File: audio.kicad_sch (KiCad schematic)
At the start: 15 parts, among them J5 FH34SRJ-6S-0.5SH(50), J6 FH34SRJ-6S-0.5SH(50), J7 Conn_01x02_Female, U6 ALC5672

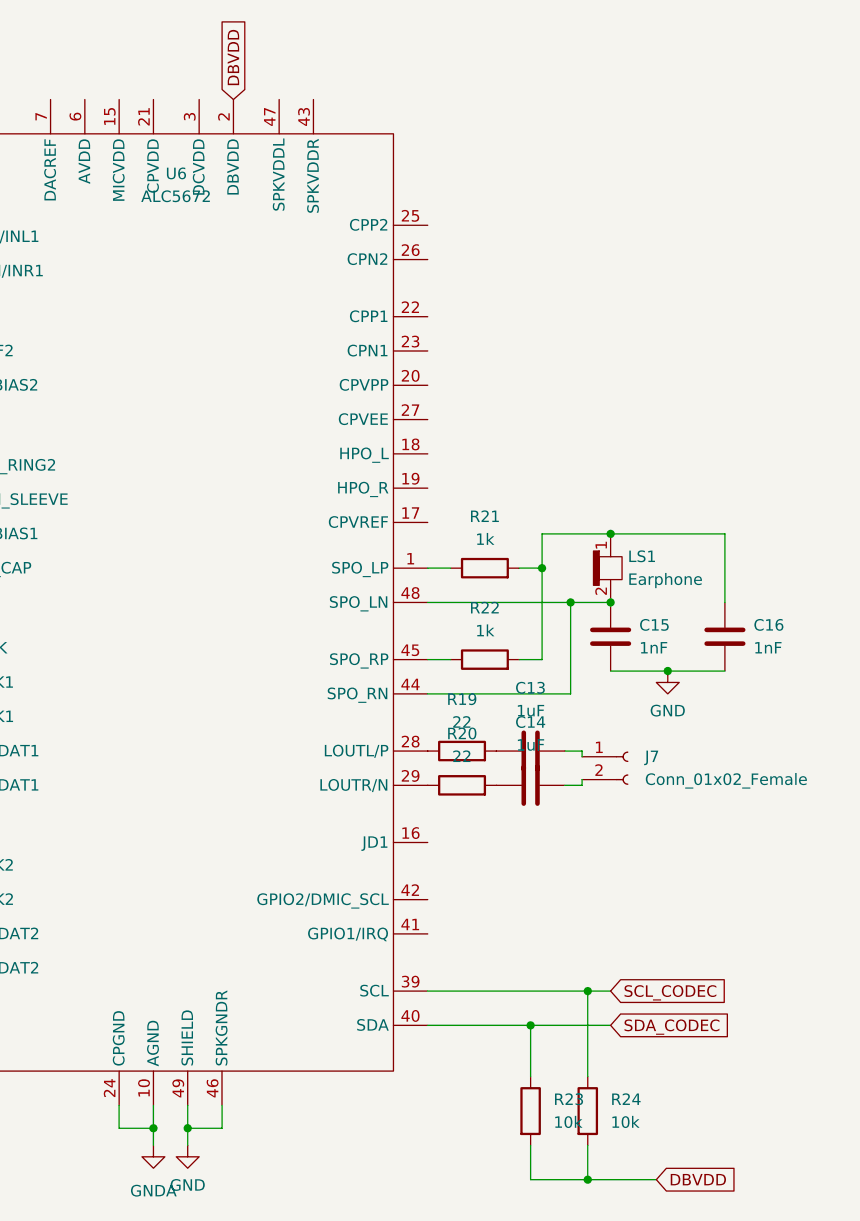
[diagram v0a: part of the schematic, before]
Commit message: USB IC Removal
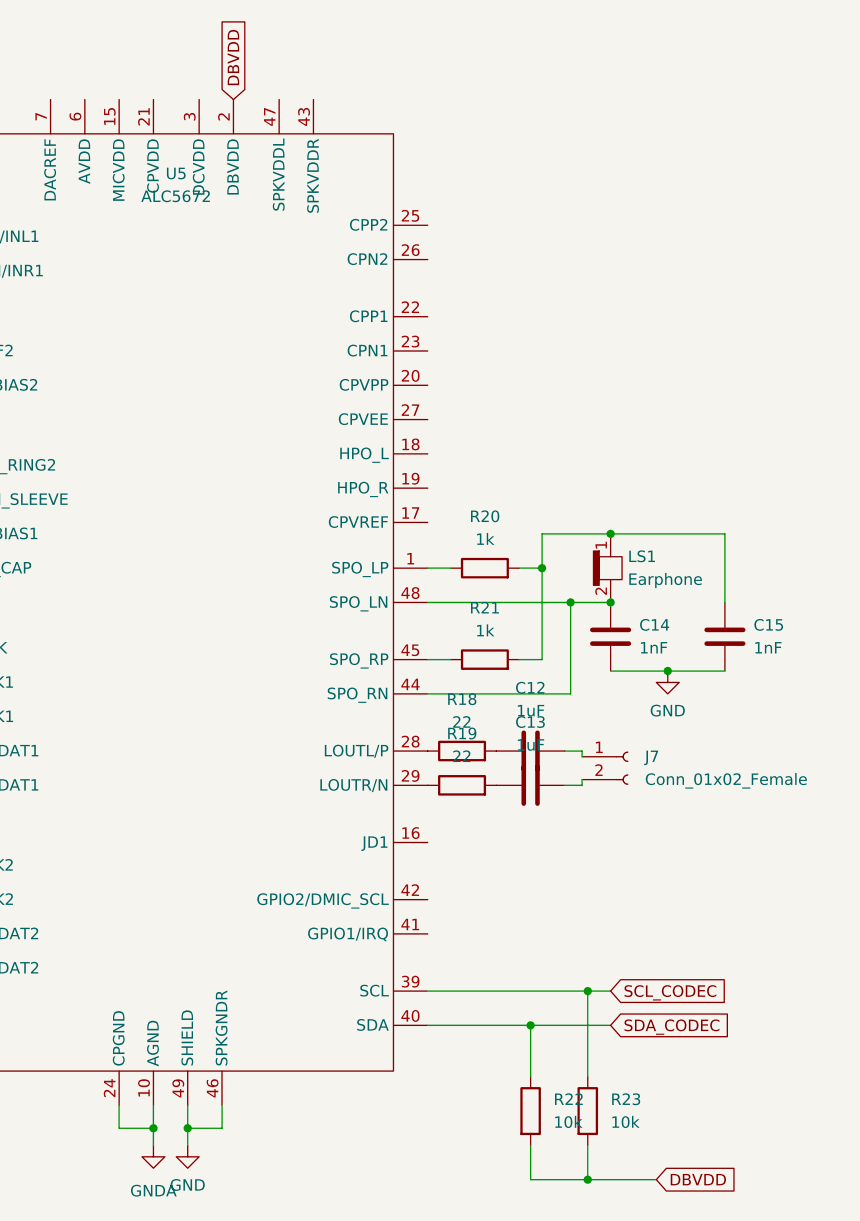
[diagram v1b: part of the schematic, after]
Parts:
- renumbered C13 to C12, C14 to C13, C15 to C14, C16 to C15, R19 to R18, R20 to R19, R21 to R20, R22 to R21, R23 to R22, R24 to R23, U6 to U5
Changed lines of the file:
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@@
   (symbol (lib_id "power:GND") (at 153.035 68.58 0) (unit 1)
     (in_bom yes) (on_board yes) (fields_autoplaced)
-    (property "Reference" "#PWR044" (id 0) (at 153.035 74.93 0)
+    (property "Reference" "#PWR041" (id 0) (at 153.035 74.93 0)
       (effects (font (size 1.27 1.27)) hide)
     )
@@
   (symbol (lib_id "Device:C") (at 256.54 100.965 90) (unit 1)
     (in_bom yes) (on_board yes) (fields_autoplaced)
-    (property "Reference" "C13" (id 0) (at 256.54 93.98 90))
+    (property "Reference" "C12" (id 0) (at 256.54 93.98 90))
     (property "Value" "1uF" (id 1) (at 256.54 96.52 90))
     (property "Footprint" "Capacitor_SMD:C_0402_1005Metric" (id 2) (at 260.35 99.9998 0)
@@
   (symbol (lib_id "Device:C") (at 256.54 104.775 90) (unit 1)
     (in_bom yes) (on_board yes) (fields_autoplaced)
-    (property "Reference" "C14" (id 0) (at 256.54 97.79 90))
+    (property "Reference" "C13" (id 0) (at 256.54 97.79 90))
     (property "Value" "1uF" (id 1) (at 256.54 100.33 90))
     (property "Footprint" "Capacitor_SMD:C_0402_1005Metric" (id 2) (at 260.35 103.8098 0)
@@
   (symbol (lib_id "Device:R") (at 251.46 80.645 90) (unit 1)
     (in_bom yes) (on_board yes) (fields_autoplaced)
-    (property "Reference" "R21" (id 0) (at 251.46 74.93 90))
+    (property "Reference" "R20" (id 0) (at 251.46 74.93 90))
     (property "Value" "1k" (id 1) (at 251.46 77.47 90))
     (property "Footprint" "Resistor_SMD:R_0402_1005Metric" (id 2) (at 251.46 82.423 90)
@@
   (symbol (lib_id "JLCPCB:ALC5672") (at 217.17 81.915 0) (unit 1)
     (in_bom yes) (on_board yes) (fields_autoplaced)
-    (property "Reference" "U6" (id 0) (at 217.17 36.83 0))
+    (property "Reference" "U5" (id 0) (at 217.17 36.83 0))
     (property "Value" "ALC5672" (id 1) (at 217.17 39.37 0))
     (property "Footprint" "JLCPCB:ALC5672-VB-CGT_QFN-48_EP_6x6_Pitch0.4mm" (id 2) (at 217.17 123.14 0)
@@
   (symbol (lib_id "power:GND") (at 132.715 71.12 0) (unit 1)
     (in_bom yes) (on_board yes) (fields_autoplaced)
-    (property "Reference" "#PWR042" (id 0) (at 132.715 77.47 0)
+    (property "Reference" "#PWR039" (id 0) (at 132.715 77.47 0)
       (effects (font (size 1.27 1.27)) hide)
     )
@@
   (symbol (lib_id "power:GND") (at 153.67 34.925 0) (unit 1)
     (in_bom yes) (on_board yes) (fields_autoplaced)
-    (property "Reference" "#PWR046" (id 0) (at 153.67 41.275 0)
+    (property "Reference" "#PWR043" (id 0) (at 153.67 41.275 0)
       (effects (font (size 1.27 1.27)) hide)
     )
@@
   (symbol (lib_id "power:GND") (at 218.44 144.78 0) (unit 1)
     (in_bom yes) (on_board yes) (fields_autoplaced)
-    (property "Reference" "#PWR049" (id 0) (at 218.44 151.13 0)
+    (property "Reference" "#PWR046" (id 0) (at 218.44 151.13 0)
       (effects (font (size 1.27 1.27)) hide)
     )
@@
   (symbol (lib_id "Device:C") (at 278.13 88.265 0) (unit 1)
     (in_bom yes) (on_board yes) (fields_autoplaced)
-    (property "Reference" "C16" (id 0) (at 281.305 86.9949 0)
+    (property "Reference" "C15" (id 0) (at 281.305 86.9949 0)
       (effects (font (size 1.27 1.27)) (justify left))
     )
@@
   (symbol (lib_id "power:GND") (at 133.35 37.465 0) (unit 1)
     (in_bom yes) (on_board yes) (fields_autoplaced)
-    (property "Reference" "#PWR043" (id 0) (at 133.35 43.815 0)
+    (property "Reference" "#PWR040" (id 0) (at 133.35 43.815 0)
       (effects (font (size 1.27 1.27)) hide)
     )
@@
   (symbol (lib_id "Device:C") (at 265.43 88.265 0) (unit 1)
     (in_bom yes) (on_board yes) (fields_autoplaced)
-    (property "Reference" "C15" (id 0) (at 268.605 86.9949 0)
+    (property "Reference" "C14" (id 0) (at 268.605 86.9949 0)
       (effects (font (size 1.27 1.27)) (justify left))
     )
@@
   (symbol (lib_id "Device:R") (at 251.46 90.805 90) (unit 1)
     (in_bom yes) (on_board yes) (fields_autoplaced)
-    (property "Reference" "R22" (id 0) (at 251.46 85.09 90))
+    (property "Reference" "R21" (id 0) (at 251.46 85.09 90))
     (property "Value" "1k" (id 1) (at 251.46 87.63 90))
     (property "Footprint" "Resistor_SMD:R_0402_1005Metric" (id 2) (at 251.46 92.583 90)
@@
   (symbol (lib_id "Device:R") (at 248.92 100.965 90) (unit 1)
     (in_bom yes) (on_board yes) (fields_autoplaced)
-    (property "Reference" "R19" (id 0) (at 248.92 95.25 90))
+    (property "Reference" "R18" (id 0) (at 248.92 95.25 90))
     (property "Value" "22" (id 1) (at 248.92 97.79 90))
     (property "Footprint" "Resistor_SMD:R_0402_1005Metric" (id 2) (at 248.92 102.743 90)
@@
   (symbol (lib_id "power:GND") (at 271.78 92.075 0) (unit 1)
     (in_bom yes) (on_board yes) (fields_autoplaced)
-    (property "Reference" "#PWR050" (id 0) (at 271.78 98.425 0)
+    (property "Reference" "#PWR047" (id 0) (at 271.78 98.425 0)
       (effects (font (size 1.27 1.27)) hide)
     )
@@
   (symbol (lib_id "Device:R") (at 262.89 140.97 0) (unit 1)
     (in_bom yes) (on_board yes) (fields_autoplaced)
-    (property "Reference" "R24" (id 0) (at 265.43 139.6999 0)
+    (property "Reference" "R23" (id 0) (at 265.43 139.6999 0)
       (effects (font (size 1.27 1.27)) (justify left))
     )
@@
   (symbol (lib_id "Device:R") (at 256.54 140.97 0) (unit 1)
     (in_bom yes) (on_board yes) (fields_autoplaced)
-    (property "Reference" "R23" (id 0) (at 259.08 139.6999 0)
+    (property "Reference" "R22" (id 0) (at 259.08 139.6999 0)
       (effects (font (size 1.27 1.27)) (justify left))
     )
@@
   (symbol (lib_id "Device:R") (at 248.92 104.775 90) (unit 1)
     (in_bom yes) (on_board yes) (fields_autoplaced)
-    (property "Reference" "R20" (id 0) (at 248.92 99.06 90))
+    (property "Reference" "R19" (id 0) (at 248.92 99.06 90))
     (property "Value" "22" (id 1) (at 248.92 101.6 90))
     (property "Footprint" "Resistor_SMD:R_0402_1005Metric" (id 2) (at 248.92 106.553 90)
@@
   (symbol (lib_id "power:GND") (at 153.035 88.9 0) (unit 1)
     (in_bom yes) (on_board yes) (fields_autoplaced)
-    (property "Reference" "#PWR045" (id 0) (at 153.035 95.25 0)
+    (property "Reference" "#PWR042" (id 0) (at 153.035 95.25 0)
       (effects (font (size 1.27 1.27)) hide)
     )
@@
   (symbol (lib_id "power:GND") (at 153.67 55.245 0) (unit 1)
     (in_bom yes) (on_board yes) (fields_autoplaced)
-    (property "Reference" "#PWR047" (id 0) (at 153.67 61.595 0)
+    (property "Reference" "#PWR044" (id 0) (at 153.67 61.595 0)
       (effects (font (size 1.27 1.27)) hide)
     )
@@
   (symbol (lib_id "power:GNDA") (at 214.63 144.78 0) (unit 1)
     (in_bom yes) (on_board yes) (fields_autoplaced)
-    (property "Reference" "#PWR048" (id 0) (at 214.63 151.13 0)
-      (effects (font (size 1.27 1.27)) hide)
-    )
+    (property "Reference" "#PWR045" (id 0) (at 214.63 151.13 0)
+      (effects (font (size 1.27 1.27)) hide)
+    )

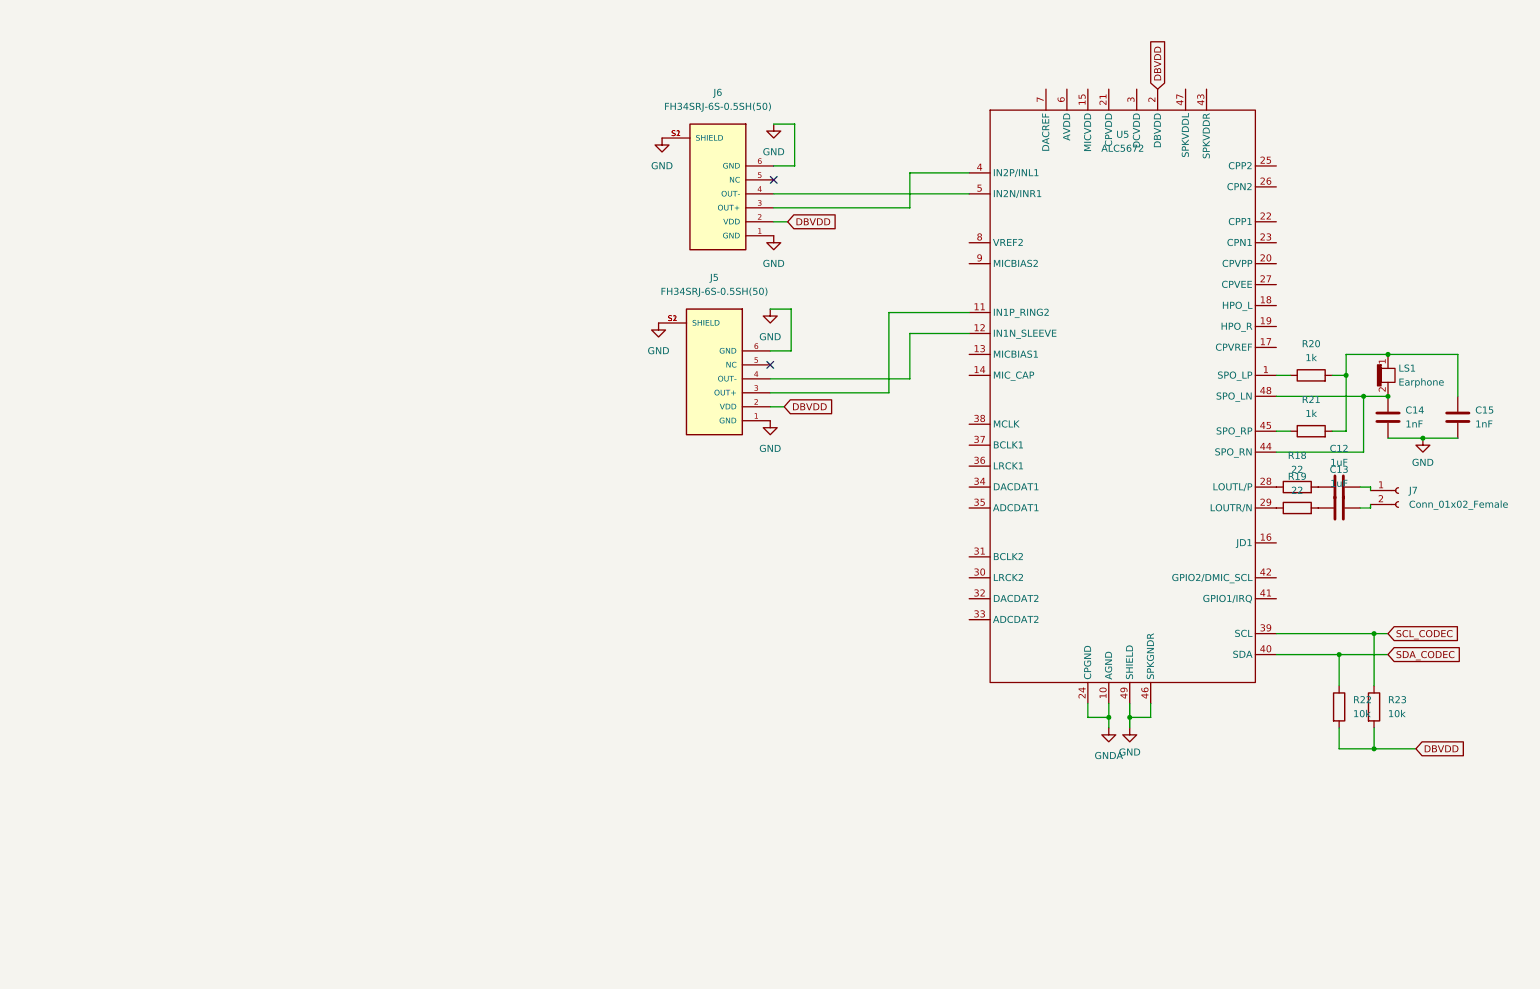
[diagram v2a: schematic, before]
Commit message: Audio near completion
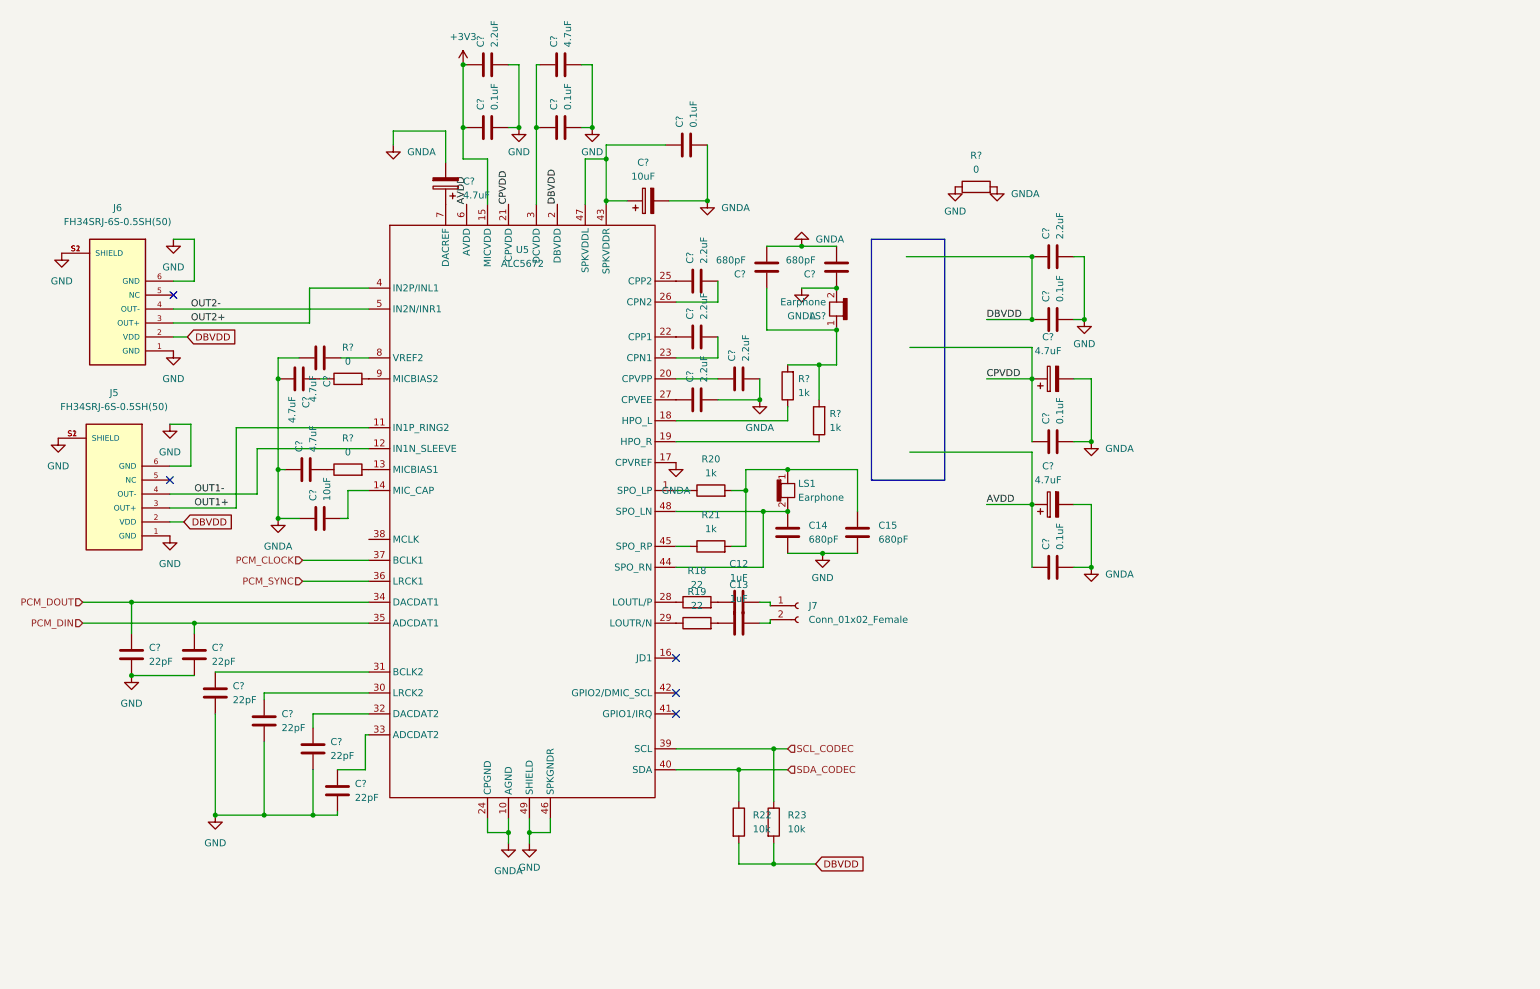
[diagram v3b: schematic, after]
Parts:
- added C? (x6): 22pF, Capacitor_SMD:C_0402_1005Metric, symbol Device:C
- added C? (x3): 4.7uF, symbol Device:C_Polarized
- added C? (x6): 0.1uF, Capacitor_SMD:C_0402_1005Metric, symbol Device:C
- added C? (x2): 680pF, Capacitor_SMD:C_0402_1005Metric, symbol Device:C
- added C?: 10uF, Capacitor_SMD:C_0402_1005Metric, symbol Device:C
- added C? (x6): 2.2uF, Capacitor_SMD:C_0402_1005Metric, symbol Device:C
- added C? (x4): 4.7uF, Capacitor_SMD:C_0402_1005Metric, symbol Device:C
- added C?: 10uF, symbol Device:C_Polarized
- added LS?: Earphone, speakerpads:speakerpads, symbol Device:Earphone
- added R? (x3): 0, Resistor_SMD:R_0402_1005Metric, symbol Device:R
- added R? (x2): 1k, Resistor_SMD:R_0402_1005Metric, symbol Device:R
- C14, C15: value 1nF -> 680pF
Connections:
- net DBVDD: now also C?.2, C?.2
- net GND: now also C?.1, C?.1, C?.1, C?.1, C?.1, C?.1, C?.1, C?.1, C?.1, C?.1, C?.1, C?.1, R?.1
- net GNDA: now also U5.17 (CPVREF), C?.1, C?.1, C?.1, C?.1, C?.1, C?.1, C?.1, C?.1, C?.2, C?.2, C?.2, C?.2, C?.2, C?.2, C?.2, C?.2, LS?.2 (+), R?.2
- net OUT1+: now reaches J5.3 (OUT+), U5.11 (IN1P_RING2)
- net OUT1-: now reaches J5.4 (OUT-), U5.12 (IN1N_SLEEVE)
- net at U5.13 (MICBIAS1): now also R?.2
- net at U5.14 (MIC_CAP): now also C?.1
- net +3V3: now reaches U5.15 (MICVDD)
- net +3V3: now also C?.2, C?.2
- net at U5.18 (HPO_L): now also R?.1
- net at U5.19 (HPO_R): now also R?.1
- net at U5.20 (CPVPP): now also C?.2
- net CPVDD: now reaches U5.21 (CPVDD)
- net CPVDD: now also C?.1, C?.2
- net at U5.22 (CPP1): now also C?.2
- net at U5.23 (CPN1): now also C?.1
- net at U5.25 (CPP2): now also C?.2
- net at U5.26 (CPN2): now also C?.1
- net at U5.27 (CPVEE): now also C?.2
- net at U5.3 (DCVDD): now also C?.2, C?.2
- net at U5.30 (LRCK2): now also C?.2
- net at U5.31 (BCLK2): now also C?.2
- net at U5.32 (DACDAT2): now also C?.2
- net at U5.33 (ADCDAT2): now also C?.2
- net PCM_DOUT: now reaches U5.34 (DACDAT1)
- net PCM_DOUT: now also C?.2
- net PCM_DIN: now reaches U5.35 (ADCDAT1)
- net PCM_DIN: now also C?.2
- net PCM_SYNC: now reaches U5.36 (LRCK1)
- net PCM_CLOCK: now reaches U5.37 (BCLK1)
- net OUT2+: now reaches J6.3 (OUT+), U5.4 (IN2P/INL1)
- net at U5.43 (SPKVDDR): now also U5.47 (SPKVDDL), C?.1, C?.2
- net OUT2-: now reaches J6.4 (OUT-), U5.5 (IN2N/INR1)
- net AVDD: now reaches U5.6 (AVDD)
- net AVDD: now also C?.1, C?.2
- net at U5.7 (DACREF): now also C?.1
- net at U5.8 (VREF2): now also C?.2
- net at U5.9 (MICBIAS2): now also R?.2
- new net: C?.2, R?.1
- new net: C?.1, LS?.1 (-), R?.2, R?.2
- new net: C?.1, R?.1
- no-connect marks 2 -> 5
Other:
- moved on the sheet: C12, C13, C14, C15, J5, J6, J7, LS1, R18, R19, R20, R21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

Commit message: All Routed!
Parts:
- added J10: +, TestPoint:TestPoint_THTPad_2.0x2.0mm_Drill1.0mm, symbol Connector_Generic:Conn_01x01
- added J11: -, TestPoint:TestPoint_THTPad_2.0x2.0mm_Drill1.0mm, symbol Connector_Generic:Conn_01x01
- C28, C33, C47, C49: renamed from C?; footprint (none) -> Capacitor_SMD:C_0402_1005Metric
- C30, C32, C34, C46, C48, C50: renamed from C?; value 0.1uF -> 100nF
- J7: renamed from J5; footprint JLCPCB:HRS_FH34SRJ-6S-0.5SH(50) -> lib_fp:HRS_FH34SRJ-6S-0.5SH(50); MANUFACTURER HRS -> (none); MPN (none) -> C224194
- J8: renamed from J6; footprint JLCPCB:HRS_FH34SRJ-6S-0.5SH(50) -> lib_fp:HRS_FH34SRJ-6S-0.5SH(50); MANUFACTURER HRS -> (none); MPN (none) -> C224194
- LS1: footprint speakerpads:speakerpads -> (none); now left out of the parts list
- R20, R21, R30: renamed from R?; now left out of the parts list
- U6: renamed from U5; footprint JLCPCB:ALC5672-VB-CGT_QFN-48_EP_6x6_Pitch0.4mm -> lib_fp:ALC5672-VB-CGT_QFN-48_EP_6x6_Pitch0.4mm; MPN (none) -> C474324
- gave numbers to parts that had none: 22
- renumbered C12 to C39, C13 to C40, C14 to C42, C15 to C44, J7 to J9, R18 to R22, R19 to R23, R20 to R24, R21 to R25, R22 to R26, R23 to R27
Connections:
- net +3V3: now also C33.1, C34.2, U6.43 (SPKVDDR), U6.47 (SPKVDDL)
- net GND: now also C33.2, C34.1, C41.2, C43.1, C43.2, LS2.2 (+)
- net GNDA: no longer C33.2, C34.1, C41.2, C43.1, C43.2, LS2.2 (+)
- net OUT1+: now also J8.3 (OUT+); no longer J7.3 (OUT+)
- net OUT1-: now also J8.4 (OUT-); no longer J7.4 (OUT-)
- net OUT2+: now also J7.3 (OUT+); no longer J8.3 (OUT+)
- net OUT2-: now also J7.4 (OUT-); no longer J8.4 (OUT-)
- net at C44.1, LS1.1 (-), R24.2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: now also J11.1 (Pin_1)
- net at C42.1, LS1.2 (+), U6.44 (SPO_RN)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: now also J10.1 (Pin_1)
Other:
- moved on the sheet: J7, J8
